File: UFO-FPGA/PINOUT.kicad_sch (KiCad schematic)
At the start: 0 parts

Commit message: Arduino PCB
Added Arduino PCB format
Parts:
- added J1: Power, Connector_PinSocket_2.54mm:PinSocket_1x08_P2.54mm_Vertical, symbol Connector_Generic:Conn_01x08
- added J2: Analog, Connector_PinSocket_2.54mm:PinSocket_1x06_P2.54mm_Vertical, symbol Connector_Generic:Conn_01x06
- added J3: Digital/PWM, Connector_PinSocket_2.54mm:PinSocket_1x10_P2.54mm_Vertical, symbol Connector_Generic:Conn_01x10
- added J4: Digital/PWM, Connector_PinSocket_2.54mm:PinSocket_1x08_P2.54mm_Vertical, symbol Connector_Generic:Conn_01x08
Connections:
- new net *10: J3.8 (Pin_8)
- new net *11: J3.7 (Pin_7)
- new net *3: J4.5 (Pin_5)
- new net *5: J4.3 (Pin_3)
- new net *6: J4.2 (Pin_2)
- new net *9: J3.9 (Pin_9)
- new net +3V3: J1.4 (Pin_4)
- new net +5V: J1.5 (Pin_5)
- new net 12: J3.6 (Pin_6)
- new net 13: J3.5 (Pin_5)
- new net 2: J4.6 (Pin_6)
- new net 4: J4.4 (Pin_4)
- new net 7: J4.1 (Pin_1)
- new net 8: J3.10 (Pin_10)
- new net A0: J2.1 (Pin_1)
- new net A1: J2.2 (Pin_2)
- new net A2: J2.3 (Pin_3)
- new net A3: J2.4 (Pin_4)
- new net AREF: J3.3 (Pin_3)
- new net GND: J1.6 (Pin_6), J1.7 (Pin_7), J3.4 (Pin_4)
- new net IOREF: J1.2 (Pin_2)
- new net RX/0: J4.8 (Pin_8)
- new net SCL/A5: J2.6 (Pin_6), J3.1 (Pin_1)
- new net SDA/A4: J2.5 (Pin_5), J3.2 (Pin_2)
- new net TX/1: J4.7 (Pin_7)
- new net VCC: J1.8 (Pin_8)
- new net ~{RESET}: J1.3 (Pin_3)
- no-connect marks 0 -> 1

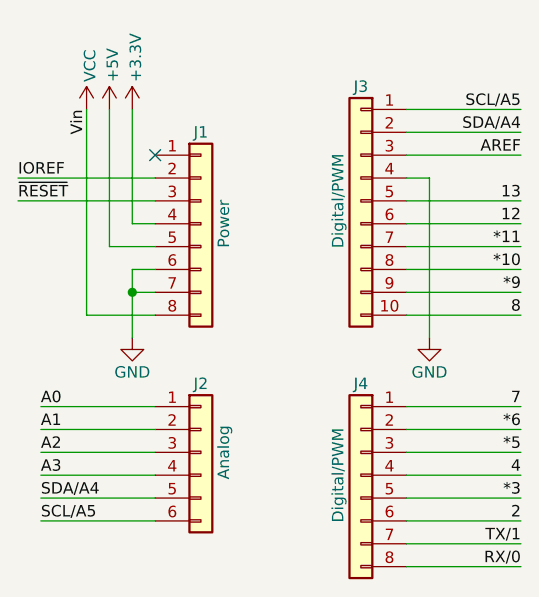
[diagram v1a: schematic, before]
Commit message: pins and USB
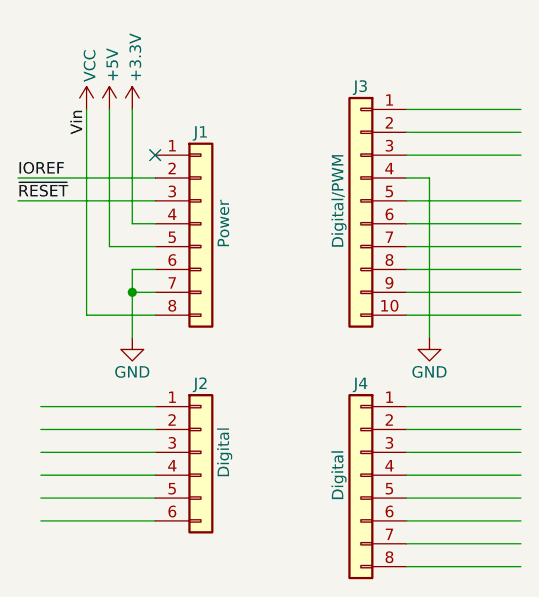
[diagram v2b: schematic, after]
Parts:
- J2: value Analog -> Digital
- J4: value Digital/PWM -> Digital
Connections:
- net *10: no longer names the net of J3.8 (Pin_8)
- net *11: no longer names the net of J3.7 (Pin_7)
- net *3: no longer names the net of J4.5 (Pin_5)
- net *5: no longer names the net of J4.3 (Pin_3)
- net *6: no longer names the net of J4.2 (Pin_2)
- net *9: no longer names the net of J3.9 (Pin_9)
- net 12: no longer names the net of J3.6 (Pin_6)
- net 13: no longer names the net of J3.5 (Pin_5)
- net 2: no longer names the net of J4.6 (Pin_6)
- net 4: no longer names the net of J4.4 (Pin_4)
- net 7: no longer names the net of J4.1 (Pin_1)
- net 8: no longer names the net of J3.10 (Pin_10)
- net A0: no longer names the net of J2.1 (Pin_1)
- net A1: no longer names the net of J2.2 (Pin_2)
- net A2: no longer names the net of J2.3 (Pin_3)
- net A3: no longer names the net of J2.4 (Pin_4)
- net AREF: no longer names the net of J3.3 (Pin_3)
- net RX/0: no longer names the net of J4.8 (Pin_8)
- net SCL/A5: no longer names the net of J2.6 (Pin_6)
- net SCL/A5: no longer J3.1 (Pin_1)
- net SDA/A4: no longer names the net of J2.5 (Pin_5)
- net SDA/A4: no longer J3.2 (Pin_2)
- net TX/1: no longer names the net of J4.7 (Pin_7)
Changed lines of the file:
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@@
     (stroke (width 0) (type solid))
-  )
-  (label "A1" (at 45.72 69.215 0) (fields_autoplaced)
-    (effects (font (size 1.27 1.27)) (justify left bottom))
-  )
-  (label "A3" (at 45.72 74.295 0) (fields_autoplaced)
-    (effects (font (size 1.27 1.27)) (justify left bottom))
-  )
-  (label "A2" (at 45.72 71.755 0) (fields_autoplaced)
-    (effects (font (size 1.27 1.27)) (justify left bottom))
-  )
-  (label "SDA{slash}A4" (at 45.72 76.835 0) (fields_autoplaced)
-    (effects (font (size 1.27 1.27)) (justify left bottom))
-  )
-  (label "*6" (at 99.06 69.215 180) (fields_autoplaced)
-    (effects (font (size 1.27 1.27)) (justify right bottom))
-  )
-  (label "*9" (at 99.06 53.975 180) (fields_autoplaced)
-    (effects (font (size 1.27 1.27)) (justify right bottom))
-  )
-  (label "8" (at 99.06 56.515 180) (fields_autoplaced)
-    (effects (font (size 1.27 1.27)) (justify right bottom))
-  )
-  (label "13" (at 99.06 43.815 180) (fields_autoplaced)
-    (effects (font (size 1.27 1.27)) (justify right bottom))
-  )
-  (label "*5" (at 99.06 71.755 180) (fields_autoplaced)
-    (effects (font (size 1.27 1.27)) (justify right bottom))
-  )
-  (label "TX{slash}1" (at 99.06 81.915 180) (fields_autoplaced)
-    (effects (font (size 1.27 1.27)) (justify right bottom))
   )
   (label "IOREF" (at 43.18 41.275 0) (fields_autoplaced)
@@
     (effects (font (size 1.27 1.27)) (justify left bottom))
   )
-  (label "AREF" (at 99.06 38.735 180) (fields_autoplaced)
-    (effects (font (size 1.27 1.27)) (justify right bottom))
-  )
   (label "Vin" (at 50.8 33.655 270) (fields_autoplaced)
-    (effects (font (size 1.27 1.27)) (justify right bottom))
-  )
-  (label "7" (at 99.06 66.675 180) (fields_autoplaced)
-    (effects (font (size 1.27 1.27)) (justify right bottom))
-  )
-  (label "4" (at 99.06 74.295 180) (fields_autoplaced)
-    (effects (font (size 1.27 1.27)) (justify right bottom))
-  )
-  (label "2" (at 99.06 79.375 180) (fields_autoplaced)
-    (effects (font (size 1.27 1.27)) (justify right bottom))
-  )
-  (label "A0" (at 45.72 66.675 0) (fields_autoplaced)
-    (effects (font (size 1.27 1.27)) (justify left bottom))
-  )
-  (label "SCL{slash}A5" (at 45.72 79.375 0) (fields_autoplaced)
-    (effects (font (size 1.27 1.27)) (justify left bottom))
-  )
-  (label "*3" (at 99.06 76.835 180) (fields_autoplaced)
-    (effects (font (size 1.27 1.27)) (justify right bottom))
-  )
-  (label "SDA{slash}A4" (at 99.06 36.195 180) (fields_autoplaced)
-    (effects (font (size 1.27 1.27)) (justify right bottom))
-  )
-  (label "*10" (at 99.06 51.435 180) (fields_autoplaced)
-    (effects (font (size 1.27 1.27)) (justify right bottom))
-  )
-  (label "RX{slash}0" (at 99.06 84.455 180) (fields_autoplaced)
-    (effects (font (size 1.27 1.27)) (justify right bottom))
-  )
-  (label "*11" (at 99.06 48.895 180) (fields_autoplaced)
-    (effects (font (size 1.27 1.27)) (justify right bottom))
-  )
-  (label "SCL{slash}A5" (at 99.06 33.655 180) (fields_autoplaced)
-    (effects (font (size 1.27 1.27)) (justify right bottom))
-  )
-  (label "12" (at 99.06 46.355 180) (fields_autoplaced)
     (effects (font (size 1.27 1.27)) (justify right bottom))
   )
@@
       (effects (font (size 1.27 1.27)))
     )
-    (property "Value" "Digital/PWM" (at 78.74 74.295 90)
+    (property "Value" "Digital" (at 78.74 74.295 90)
       (effects (font (size 1.27 1.27)))
     )
@@
       (effects (font (size 1.27 1.27)))
     )
-    (property "Value" "Analog" (at 66.04 71.755 90)
+    (property "Value" "Digital" (at 66.04 71.755 90)
       (effects (font (size 1.27 1.27)))
     )

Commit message: De inverting supply schakeling gemaakt
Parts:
- removed J1: Power, Connector_PinSocket_2.54mm:PinSocket_1x08_P2.54mm_Vertical, symbol Connector_Generic:Conn_01x08
- removed J2: Digital, Connector_PinSocket_2.54mm:PinSocket_1x06_P2.54mm_Vertical, symbol Connector_Generic:Conn_01x06
- removed J3: Digital/PWM, Connector_PinSocket_2.54mm:PinSocket_1x10_P2.54mm_Vertical, symbol Connector_Generic:Conn_01x10
- removed J4: Digital, Connector_PinSocket_2.54mm:PinSocket_1x08_P2.54mm_Vertical, symbol Connector_Generic:Conn_01x08
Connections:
- no-connect marks 1 -> 0
